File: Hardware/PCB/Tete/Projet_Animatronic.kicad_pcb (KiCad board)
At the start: 2 copper layers, 28 parts, among them J1 Conn_01x06, J2 Conn_01x06, J3 Conn_01x06, J4 Conn_01x15, U8 PCA9685PW

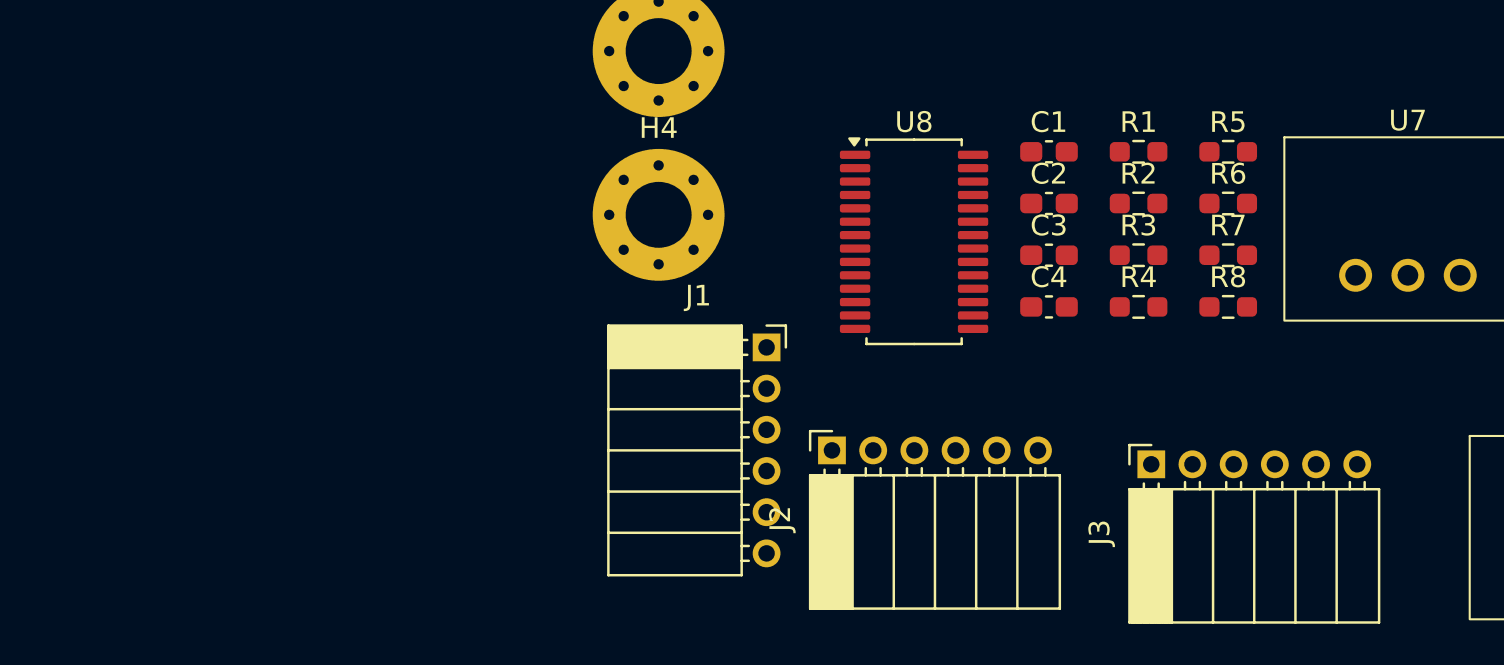
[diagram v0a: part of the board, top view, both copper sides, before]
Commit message: change i2c addr led driver conf
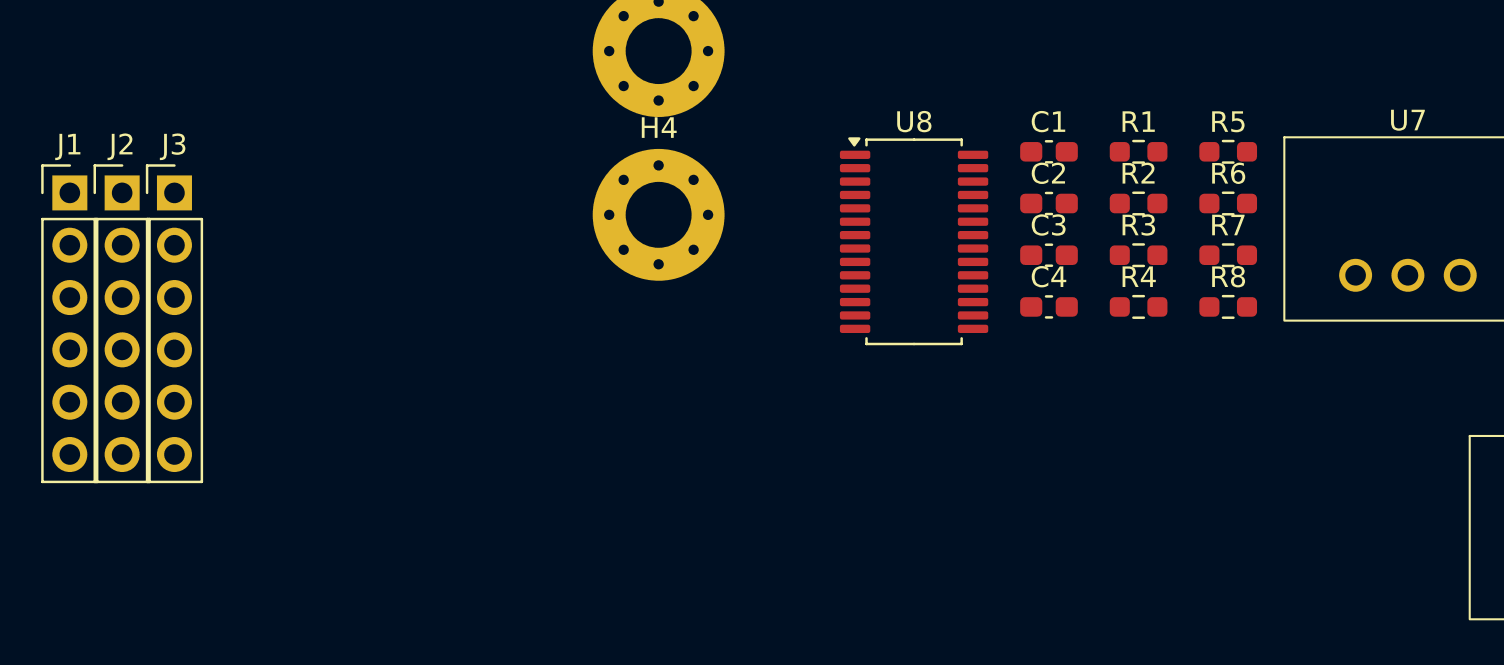
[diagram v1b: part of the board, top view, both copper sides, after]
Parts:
- J1, J2, J3: footprint Connector_PinSocket_2.00mm:PinSocket_1x06_P2.00mm_Horizontal -> Connector_PinHeader_2.54mm:PinHeader_1x06_P2.54mm_Vertical
- moved J3 49.2 mm to (105.1, 100.0), turned to 0 degrees
- moved J2 36.7 mm to (102.5, 100.0), turned to 0 degrees
- moved J1 34.6 mm to (100.0, 100.0)
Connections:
- C1 pad 1: PWM_TIM1_CH1 -> +5V
- C2 pad 1: PWM_TIM1_CH1 -> +5V
- C3 pad 1: PWM_TIM1_CH1 -> +5V
- C4 pad 1: PWM_TIM1_CH1 -> +5V
- J1 pad 2: PWM_TIM1_CH1 -> PWM_TIM1_CH2
- J1 pad 3: PWM_TIM1_CH1 -> PWM_TIM1_CH3
- J1 pad 4: PWM_TIM1_CH1 -> PWM_TIM1_CH4
- J1 pad 5: PWM_TIM1_CH1 -> PWM_TIM2_CH1
- J1 pad 6: PWM_TIM1_CH1 -> PWM_TIM2_CH2
- J2 pad 1: PWM_TIM1_CH1 -> +5V
- J2 pad 2: PWM_TIM1_CH1 -> +5V
- J2 pad 3: PWM_TIM1_CH1 -> +5V
- J2 pad 4: PWM_TIM1_CH1 -> +5V
- J2 pad 5: PWM_TIM1_CH1 -> +5V
- J2 pad 6: PWM_TIM1_CH1 -> +5V
- J4 pad 3: PWM_TIM1_CH1 -> PWM_TIM1_CH2
- J4 pad 4: PWM_TIM1_CH1 -> PWM_TIM1_CH3
- J4 pad 5: PWM_TIM1_CH1 -> PWM_TIM1_CH4
- J4 pad 6: PWM_TIM1_CH1 -> PWM_TIM2_CH1
- J4 pad 7: PWM_TIM1_CH1 -> PWM_TIM2_CH2
- R3 pad 2: PWM_TIM1_CH1 -> +5V
- R4 pad 2: PWM_TIM1_CH1 -> +5V
- R5 pad 2: PWM_TIM1_CH1 -> +5V
- R6 pad 2: PWM_TIM1_CH1 -> +5V
- R7 pad 2: PWM_TIM1_CH1 -> +5V
- R8 pad 2: PWM_TIM1_CH1 -> +5V
- U1 pad 2: PWM_TIM1_CH1 -> +5V
- U2 pad 2: PWM_TIM1_CH1 -> +5V
- U3 pad 2: PWM_TIM1_CH1 -> +5V
- U4 pad 2: PWM_TIM1_CH1 -> +5V
- U5 pad 2: PWM_TIM1_CH1 -> +5V
- U6 pad 2: PWM_TIM1_CH1 -> +5V
- U7 pad 2: PWM_TIM1_CH1 -> +5V
- U8 pad 1: PWM_TIM1_CH1 -> +5V
- U8 pad 28: PWM_TIM1_CH1 -> +5V
- U8 pad 3: PWM_TIM1_CH1 -> +5V
- U8 pad 5: PWM_TIM1_CH1 -> +5V
